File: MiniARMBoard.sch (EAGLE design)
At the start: 39 parts, among them CN1 ZX62-AB-5PA, U1 LPC1549JBD48, U2 TPD4S014DSQR, U3 MCP1700T-33, U4 ADR5041, U5 FT234XD-R, X1 FA238V

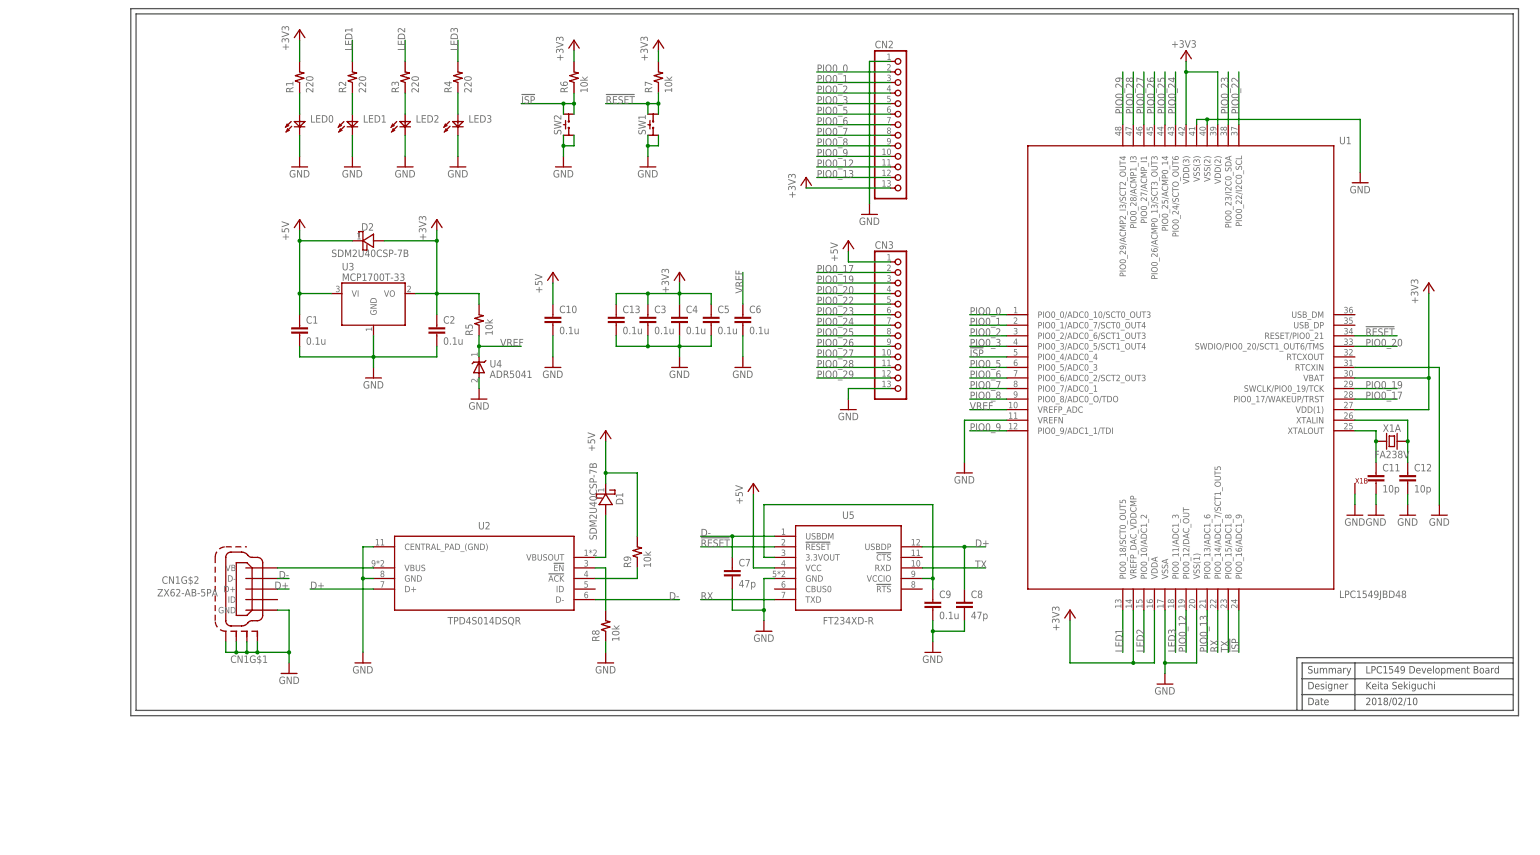
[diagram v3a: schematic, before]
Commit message: [fix]usb-dfu仕様に変更
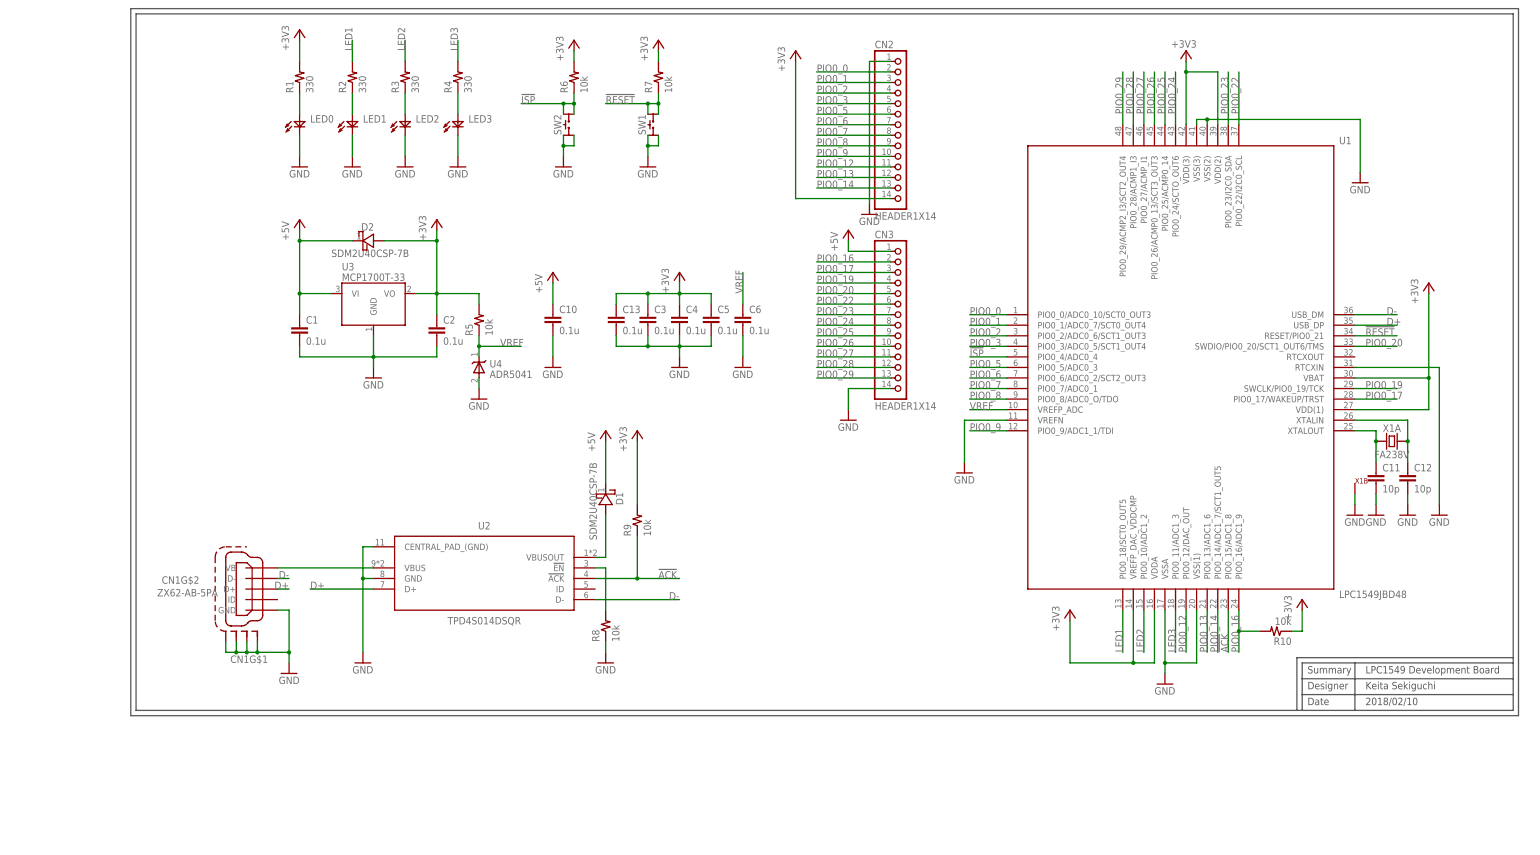
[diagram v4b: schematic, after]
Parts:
- removed C7, C8: 47p, MotorDriver:C1005
- removed C9: 0.1u, MotorDriver:C1005
- removed U5: FT234XD-R, FT234XD-R:FT234XD-R
- added R10: 10k, MotorDriver:R1005
- CN2, CN3: value (none) -> HEADER1X14; device nonolith:HEADER-1X13 -> nonolith:HEADER1X14
- R1, R2, R3, R4: value 220 -> 330
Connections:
- removed net N$4: C9.1, U5.3.3VOUT, U5.VCCIO
- removed net N$7: R9.1, U2.!ACK
- removed net RX: U1.PIO0_14/ADC1_7/SCT1_OUT5, U5.TXD
- removed net TX: U1.PIO0_15/ADC1_8, U5.RXD
- new net !ACK: R9.1, U1.PIO0_15/ADC1_8, U2.!ACK
- new net PIO0_14: CN2.13, U1.PIO0_14/ADC1_7/SCT1_OUT5
- new net PIO0_16: CN3.2, R10.2, U1.PIO0_16/ADC1_9
- net !ISP: no longer U1.PIO0_16/ADC1_9
- net !RESET: no longer U5.!RESET
- net +3V3: now also CN2.14, R10.1, R9.2; no longer CN2.13
- net +5V: no longer R9.2, U5.VCC
- net D+: now also U1.USB_DP; no longer C8.1, U5.USBDP
- net D-: now also U1.USB_DM; no longer C7.1, U5.USBDM
- net GND: now also CN3.14; no longer C7.2, C8.2, C9.2, CN3.13, U5.GND
- net PIO0_17: now also CN3.3; no longer CN3.2
- net PIO0_19: now also CN3.4; no longer CN3.3
- net PIO0_20: now also CN3.5; no longer CN3.4
- net PIO0_22: now also CN3.6; no longer CN3.5
- net PIO0_23: now also CN3.7; no longer CN3.6
- net PIO0_24: now also CN3.8; no longer CN3.7
- net PIO0_25: now also CN3.9; no longer CN3.8
- net PIO0_26: now also CN3.10; no longer CN3.9
- net PIO0_27: now also CN3.11; no longer CN3.10
- net PIO0_28: now also CN3.12; no longer CN3.11
- net PIO0_29: now also CN3.13; no longer CN3.12
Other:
- moved on the sheet: R9
